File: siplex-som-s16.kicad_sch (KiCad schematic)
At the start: 1 part, among them J1 RFShield_OnePiece

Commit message: Add power
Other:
- sheet MCU ports: added LTDC_B[0..7], LTDC_CLK, LTDC_DE, LTDC_G[0..7], LTDC_HSYNC, LTDC_R[0..7], LTDC_VSYNC, USB_DN, USB_DP, USB_VBUS_DET; removed none
- moved on the sheet: J1

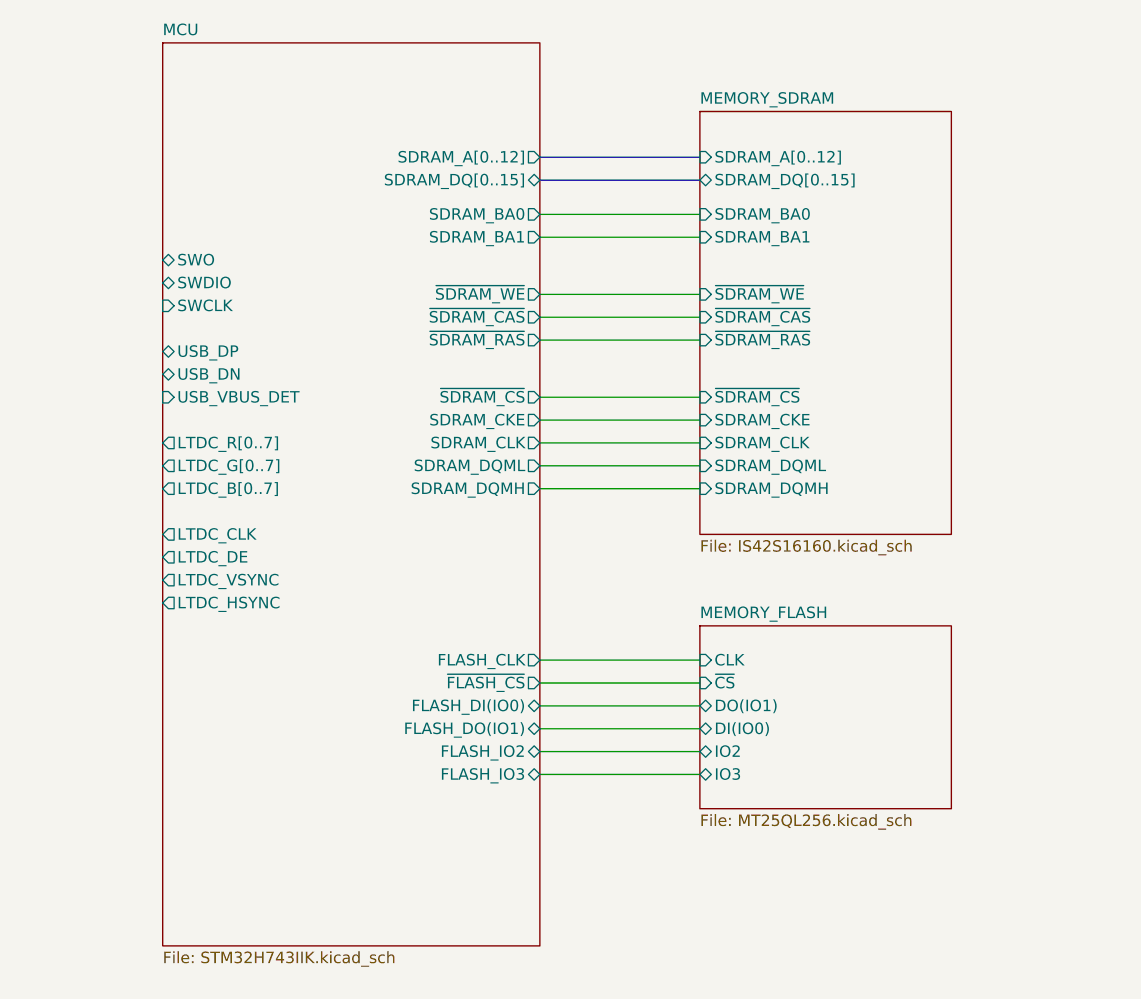
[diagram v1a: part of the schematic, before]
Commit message: Finished SDRAM, QSPI FLASH (trace length not matched yet)
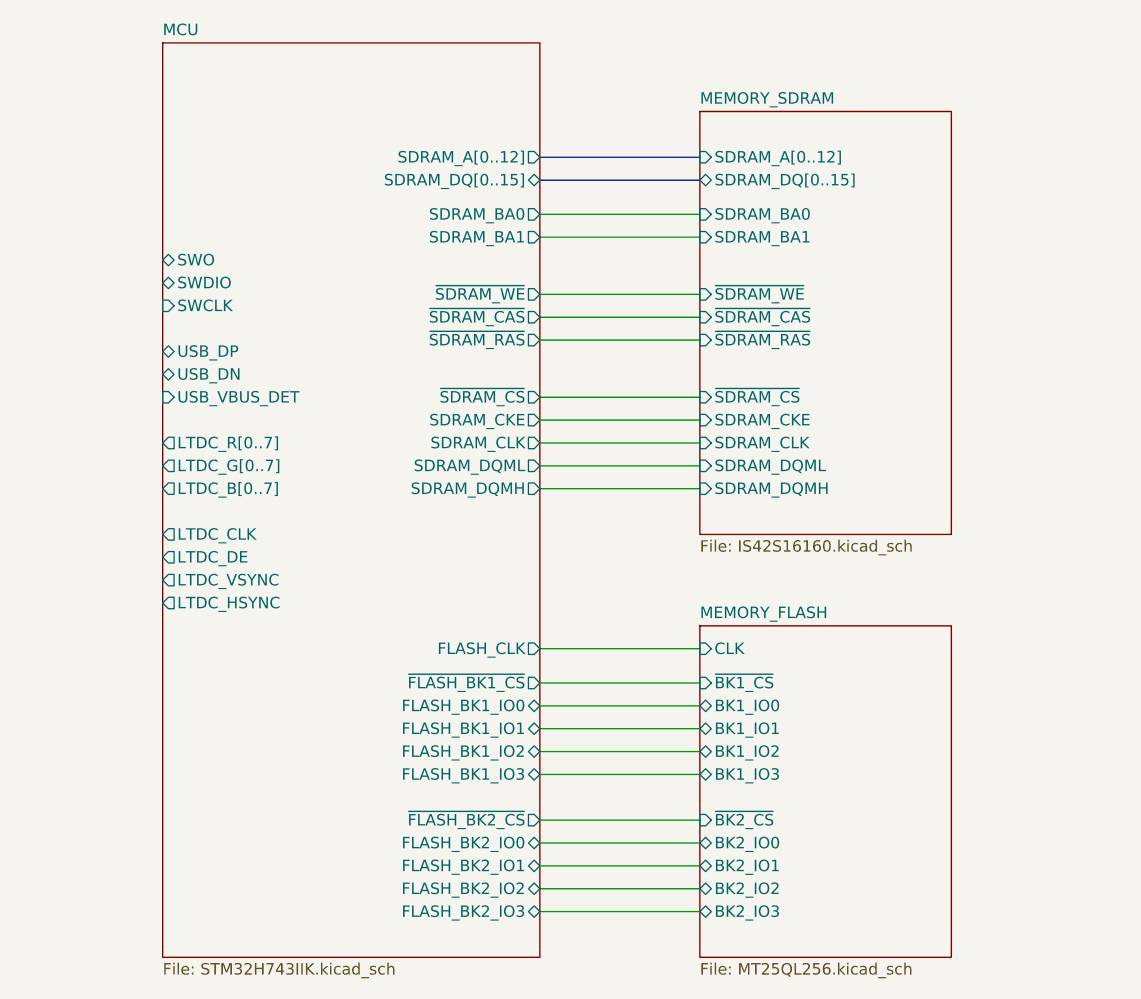
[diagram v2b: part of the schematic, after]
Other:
- sheet MCU ports: added FLASH_BK1_IO0, FLASH_BK1_IO1, FLASH_BK1_IO2, FLASH_BK1_IO3, FLASH_BK2_IO0, FLASH_BK2_IO1, FLASH_BK2_IO2, FLASH_BK2_IO3, ~{FLASH_BK1_CS}, ~{FLASH_BK2_CS}; removed FLASH_DI(IO0), FLASH_DO(IO1), FLASH_IO2, FLASH_IO3, ~{FLASH_CS}
- sheet MEMORY_FLASH ports: added BK1_IO0, BK1_IO1, BK1_IO2, BK1_IO3, BK2_IO0, BK2_IO1, BK2_IO2, BK2_IO3, ~{BK1_CS}, ~{BK2_CS}; removed DI(IO0), DO(IO1), IO2, IO3, ~{CS}
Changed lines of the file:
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@@
+	(wire
+		(pts
+			(xy 154.94 88.9) (xy 172.72 88.9)
+		)
+		(stroke
+			(width 0)
+			(type default)
+		)
+	)
 	(wire
 		(pts
@@
 	(wire
 		(pts
+			(xy 154.94 85.09) (xy 172.72 85.09)
+		)
+		(stroke
+			(width 0)
+			(type default)
+		)
+	)
+	(wire
+		(pts
+			(xy 154.94 106.68) (xy 172.72 106.68)
+		)
+		(stroke
+			(width 0)
+			(type default)
+		)
+	)
+	(wire
+		(pts
 			(xy 154.94 91.44) (xy 172.72 91.44)
 		)
@@
 	(wire
 		(pts
+			(xy 154.94 96.52) (xy 172.72 96.52)
+		)
+		(stroke
+			(width 0)
+			(type default)
+		)
+	)
+	(wire
+		(pts
 			(xy 154.94 67.31) (xy 172.72 67.31)
 		)
@@
 	(wire
 		(pts
+			(xy 154.94 111.76) (xy 172.72 111.76)
+		)
+		(stroke
+			(width 0)
+			(type default)
+		)
+	)
+	(wire
+		(pts
 			(xy 154.94 36.83) (xy 172.72 36.83)
 		)
@@
 	(wire
 		(pts
-			(xy 154.94 86.36) (xy 172.72 86.36)
+			(xy 154.94 45.72) (xy 172.72 45.72)
+		)
+		(stroke
+			(width 0)
+			(type default)
+		)
+	)
+	(wire
+		(pts
+			(xy 154.94 104.14) (xy 172.72 104.14)
 		)
 		(stroke
@@
 	(wire
 		(pts
-			(xy 154.94 45.72) (xy 172.72 45.72)
+			(xy 154.94 114.3) (xy 172.72 114.3)
 		)
 		(stroke
@@
 	(wire
 		(pts
-			(xy 154.94 88.9) (xy 172.72 88.9)
+			(xy 154.94 109.22) (xy 172.72 109.22)
 		)
 		(stroke
@@
 	(wire
 		(pts
+			(xy 154.94 93.98) (xy 172.72 93.98)
+		)
+		(stroke
+			(width 0)
+			(type default)
+		)
+	)
+	(wire
+		(pts
 			(xy 154.94 50.8) (xy 172.72 50.8)
 		)
@@
 	(wire
 		(pts
-			(xy 154.94 96.52) (xy 172.72 96.52)
-		)
-		(stroke
-			(width 0)
-			(type default)
-		)
-	)
-	(wire
-		(pts
 			(xy 154.94 57.15) (xy 172.72 57.15)
-		)
-		(stroke
-			(width 0)
-			(type default)
-		)
-	)
-	(wire
-		(pts
-			(xy 154.94 93.98) (xy 172.72 93.98)
 		)
 		(stroke
@@
 	(sheet
 		(at 113.03 17.78)
-		(size 41.91 100.33)
+		(size 41.91 101.6)
 		(fields_autoplaced yes)
 		(stroke
@@
 		)
 		(property "Sheetfile" "STM32H743IIK.kicad_sch"
-			(at 113.03 118.6946 0)
+			(at 113.03 119.9646 0)
 			(effects
 				(font
@@
 			)
 		)
-		(pin "FLASH_IO2" bidirectional
-			(at 154.94 96.52 0)
-			(effects
-				(font
-					(size 1.27 1.27)
-				)
-				(justify right)
-			)
-		)
-		(pin "FLASH_IO3" bidirectional
-			(at 154.94 99.06 0)
-			(effects
-				(font
-					(size 1.27 1.27)
-				)
-				(justify right)
-			)
-		)
-		(pin "FLASH_DI(IO0)" bidirectional
-			(at 154.94 91.44 0)
-			(effects
-				(font
-					(size 1.27 1.27)
-				)
-				(justify right)
-			)
-		)
-		(pin "FLASH_CLK" output
-			(at 154.94 86.36 0)
-			(effects
-				(font
-					(size 1.27 1.27)
-				)
-				(justify right)
-			)
-		)
-		(pin "~{FLASH_CS}" output
-			(at 154.94 88.9 0)
-			(effects
-				(font
-					(size 1.27 1.27)
-				)
-				(justify right)
-			)
-		)
-		(pin "FLASH_DO(IO1)" bidirectional
-			(at 154.94 93.98 0)
-			(effects
-				(font
-					(size 1.27 1.27)
-				)
-				(justify right)
-			)
-		)
 		(pin "LTDC_R[0..7]" output
 			(at 113.03 62.23 180)
@@
 				)
 				(justify left)
+			)
+		)
+		(pin "FLASH_BK2_IO1" bidirectional
+			(at 154.94 109.22 0)
+			(effects
+				(font
+					(size 1.27 1.27)
+				)
+				(justify right)
+			)
+		)
+		(pin "FLASH_BK2_IO0" bidirectional
+			(at 154.94 106.68 0)
+			(effects
+				(font
+					(size 1.27 1.27)
+				)
+				(justify right)
+			)
+		)
+		(pin "FLASH_CLK" output
+			(at 154.94 85.09 0)
+			(effects
+				(font
+					(size 1.27 1.27)
+				)
+				(justify right)
+			)
+		)
+		(pin "~{FLASH_BK1_CS}" output
+			(at 154.94 88.9 0)
+			(effects
+				(font
+					(size 1.27 1.27)
+				)
+				(justify right)
+			)
+		)
+		(pin "FLASH_BK2_IO2" bidirectional
+			(at 154.94 111.76 0)
+			(effects
+				(font
+					(size 1.27 1.27)
+				)
+				(justify right)
+			)
+		)
+		(pin "FLASH_BK2_IO3" bidirectional
+			(at 154.94 114.3 0)
+			(effects
+				(font
+					(size 1.27 1.27)
+				)
+				(justify right)
+			)
+		)
+		(pin "FLASH_BK1_IO0" bidirectional
+			(at 154.94 91.44 0)
+			(effects
+				(font
+					(size 1.27 1.27)
+				)
+				(justify right)
+			)
+		)
+		(pin "FLASH_BK1_IO1" bidirectional
+			(at 154.94 93.98 0)
+			(effects
+				(font
+					(size 1.27 1.27)
+				)
+				(justify right)
+			)
+		)
+		(pin "FLASH_BK1_IO2" bidirectional
+			(at 154.94 96.52 0)
+			(effects
+				(font
+					(size 1.27 1.27)
+				)
+				(justify right)
+			)
+		)
+		(pin "FLASH_BK1_IO3" bidirectional
+			(at 154.94 99.06 0)
+			(effects
+				(font
+					(size 1.27 1.27)
+				)
+				(justify right)
+			)
+		)
+		(pin "~{FLASH_BK2_CS}" output
+			(at 154.94 104.14 0)
+			(effects
+				(font
+					(size 1.27 1.27)
+				)
+				(justify right)
 			)
 		)
@@
 	(sheet
 		(at 172.72 82.55)
-		(size 27.94 20.32)
+		(size 27.94 36.83)
 		(fields_autoplaced yes)
 		(stroke
@@
 		)
 		(property "Sheetfile" "MT25QL256.kicad_sch"
-			(at 172.72 103.4546 0)
+			(at 172.72 119.9646 0)
 			(effects
 				(font
@@
 			)
 		)
-		(pin "IO3" bidirectional
+		(pin "BK2_IO2" bidirectional
+			(at 172.72 111.76 180)
+			(effects
+				(font
+					(size 1.27 1.27)
+				)
+				(justify left)
+			)
+		)
+		(pin "BK2_IO0" bidirectional
+			(at 172.72 106.68 180)
+			(effects
+				(font
+					(size 1.27 1.27)
+				)
+				(justify left)
+			)
+		)
+		(pin "~{BK2_CS}" input
+			(at 172.72 104.14 180)
+			(effects
+				(font
+					(size 1.27 1.27)
+				)
+				(justify left)
+			)
+		)
+		(pin "BK2_IO1" bidirectional
+			(at 172.72 109.22 180)
+			(effects
+				(font
+					(size 1.27 1.27)
+				)
+				(justify left)
+			)
+		)
+		(pin "CLK" input
+			(at 172.72 85.09 180)
+			(effects
+				(font
+					(size 1.27 1.27)
+				)
+				(justify left)
+			)
+		)
+		(pin "BK2_IO3" bidirectional
+			(at 172.72 114.3 180)
+			(effects
+				(font
+					(size 1.27 1.27)
+				)
+				(justify left)
+			)
+		)
+		(pin "BK1_IO2" bidirectional
+			(at 172.72 96.52 180)
+			(effects
+				(font
+					(size 1.27 1.27)
+				)
+				(justify left)
+			)
+		)
+		(pin "~{BK1_CS}" input
+			(at 172.72 88.9 180)
+			(effects
+				(font
+					(size 1.27 1.27)
+				)
+				(justify left)
+			)
+		)
+		(pin "BK1_IO0" bidirectional
+			(at 172.72 91.44 180)
+			(effects
+				(font
+					(size 1.27 1.27)
+				)
+				(justify left)
+			)
+		)
+		(pin "BK1_IO1" bidirectional
+			(at 172.72 93.98 180)
+			(effects
+				(font
+					(size 1.27 1.27)
+				)
+				(justify left)
+			)
+		)
+		(pin "BK1_IO3" bidirectional
 			(at 172.72 99.06 180)
 			(effects
 				(font
-					(size 1.27 1.27)
-				)
-				(justify left)
-			)
-		)
-		(pin "IO2" bidirectional
-			(at 172.72 96.52 180)
-			(effects
-				(font
-					(size 1.27 1.27)
-				)
-				(justify left)
-			)
-		)
-		(pin "DO(IO1)" bidirectional
-			(at 172.72 91.44 180)
-			(effects
-				(font
-					(size 1.27 1.27)
-				)
-				(justify left)
-			)
-		)
-		(pin "~{CS}" input
-			(at 172.72 88.9 180)
-			(effects
-				(font
-					(size 1.27 1.27)
-				)
-				(justify left)
-			)
-		)
-		(pin "CLK" input
-			(at 172.72 86.36 180)
-			(effects
-				(font
-					(size 1.27 1.27)
-				)
-				(justify left)
-			)
-		)
-		(pin "DI(IO0)" bidirectional
-			(at 172.72 93.98 180)
-			(effects
-				(font

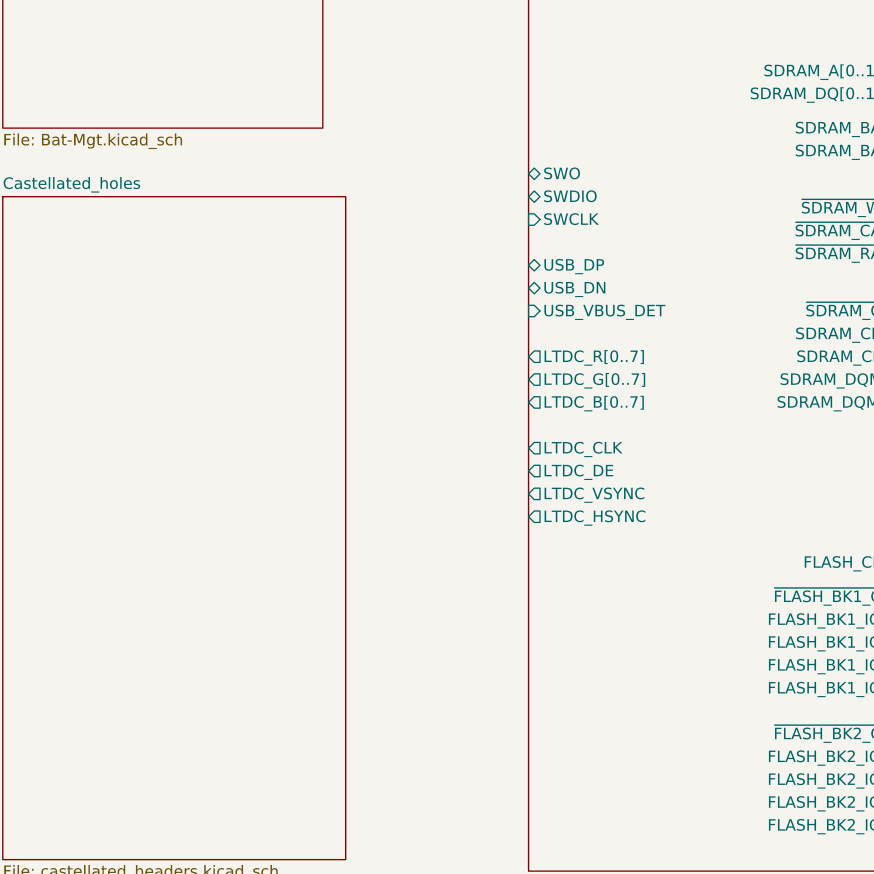
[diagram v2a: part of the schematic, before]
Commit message: Finished LTDC tracks
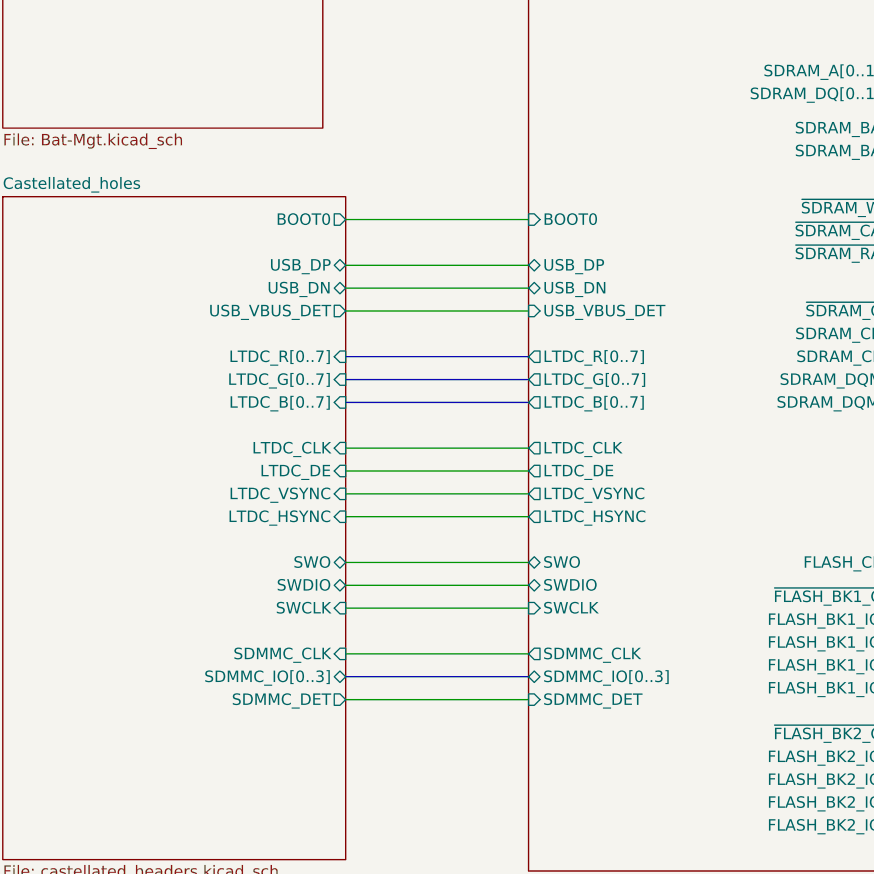
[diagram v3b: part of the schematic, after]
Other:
- sheet Castellated_holes ports: added BOOT0, LTDC_B[0..7], LTDC_CLK, LTDC_DE, LTDC_G[0..7], LTDC_HSYNC, LTDC_R[0..7], LTDC_VSYNC, SDMMC_CLK, SDMMC_DET, SDMMC_IO[0..3], SWCLK, SWDIO, SWO, USB_DN, USB_DP, USB_VBUS_DET; removed none
- sheet MCU ports: added BOOT0, SDMMC_CLK, SDMMC_DET, SDMMC_IO[0..3]; removed none

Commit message: test remote connection
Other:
- sheet Castellated_holes ports: added SDMMC_CMD; removed none
- sheet MCU ports: added SDMMC_CMD; removed none
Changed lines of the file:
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@@
+		)
+	)
+	(wire
+		(pts
+			(xy 92.71 102.87) (xy 113.03 102.87)
+		)
+		(stroke
+			(width 0)
+			(type default)
 		)
 	)
@@
 		)
 		(pin "SDMMC_DET" input
-			(at 113.03 100.33 180)
+			(at 113.03 102.87 180)
 			(effects
 				(font
@@
 		(pin "BOOT0" input
 			(at 113.03 46.99 180)
+			(effects
+				(font
+					(size 1.27 1.27)
+				)
+				(justify left)
+			)
+		)
+		(pin "SDMMC_CMD" output
+			(at 113.03 100.33 180)
 			(effects
 				(font
@@
 		)
 		(pin "SDMMC_DET" output
-			(at 92.71 100.33 0)
+			(at 92.71 102.87 0)
 			(effects
 				(font
@@
 			(effects
 				(font
+					(size 1.27 1.27)
+				)
+				(justify right)
+			)
+		)
+		(pin "SDMMC_CMD" input
+			(at 92.71 100.33 0)
+			(effects
+				(font

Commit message: generate doc
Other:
- sheet MCU ports: added NRST; removed none
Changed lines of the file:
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@@
+			)
+		)
+		(pin "NRST" input
+			(at 113.03 49.53 180)
+			(effects
+				(font
+					(size 1.27 1.27)
+				)
+				(justify left)
 			)
 		)
